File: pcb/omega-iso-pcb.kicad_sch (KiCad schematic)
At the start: 188 parts

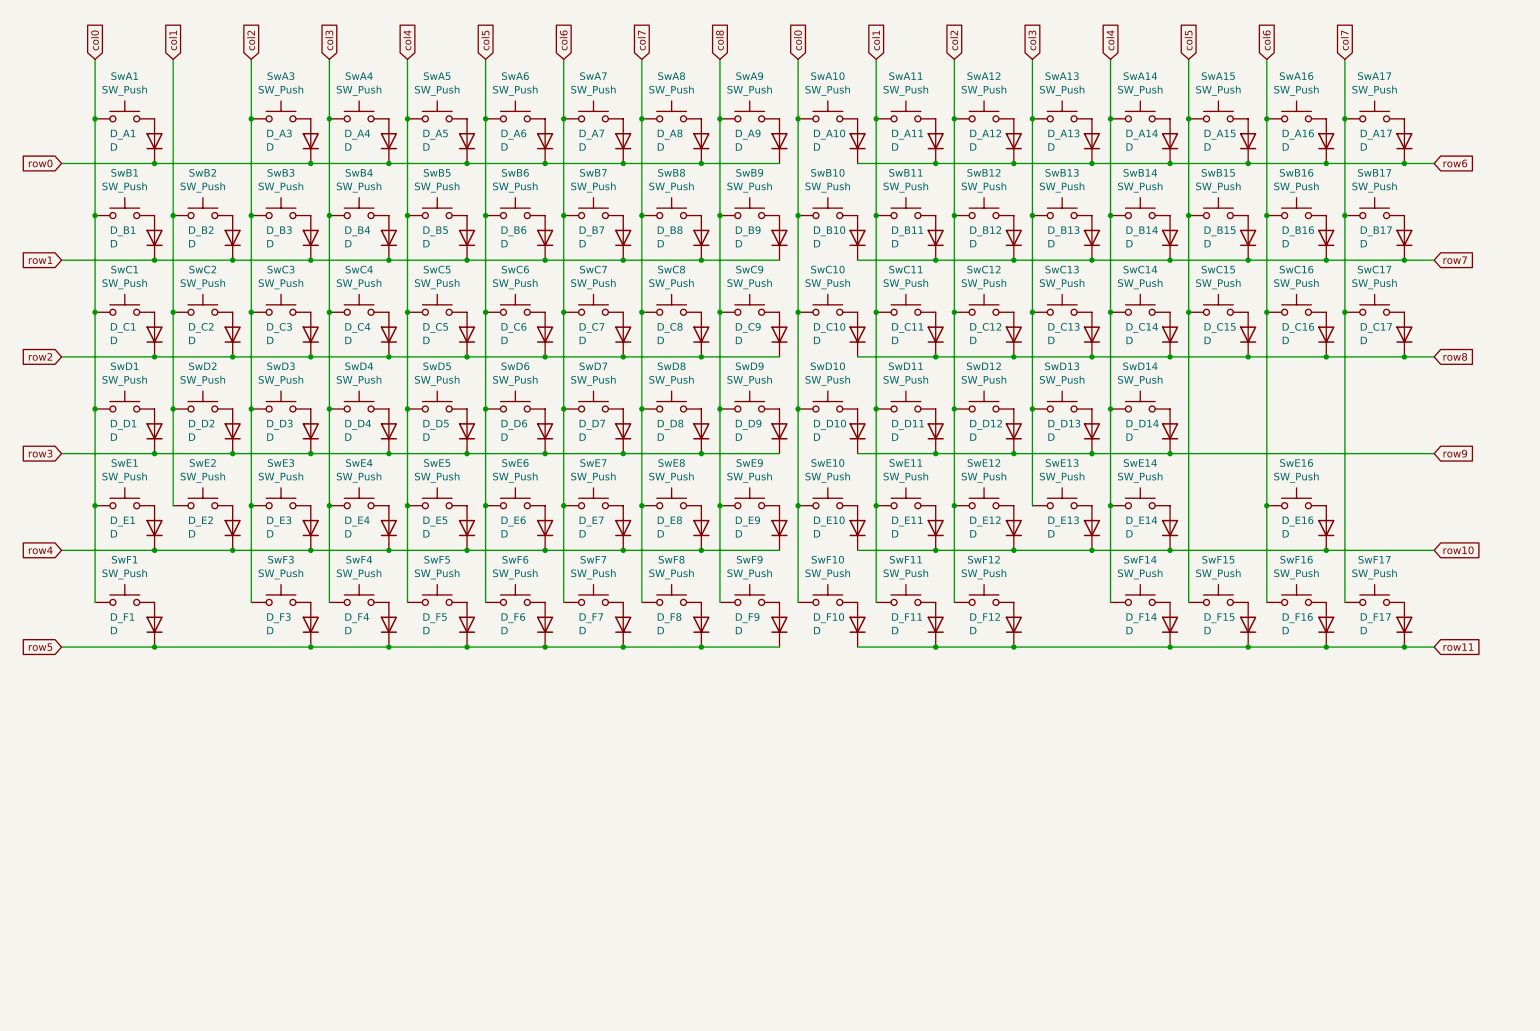
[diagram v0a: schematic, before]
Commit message: OmegaISO v0.9
* WKL TKL-like layout
* Hotswappable
* 4 up facing RGB modules for logo backlight
* Based on the Frood microcontroller
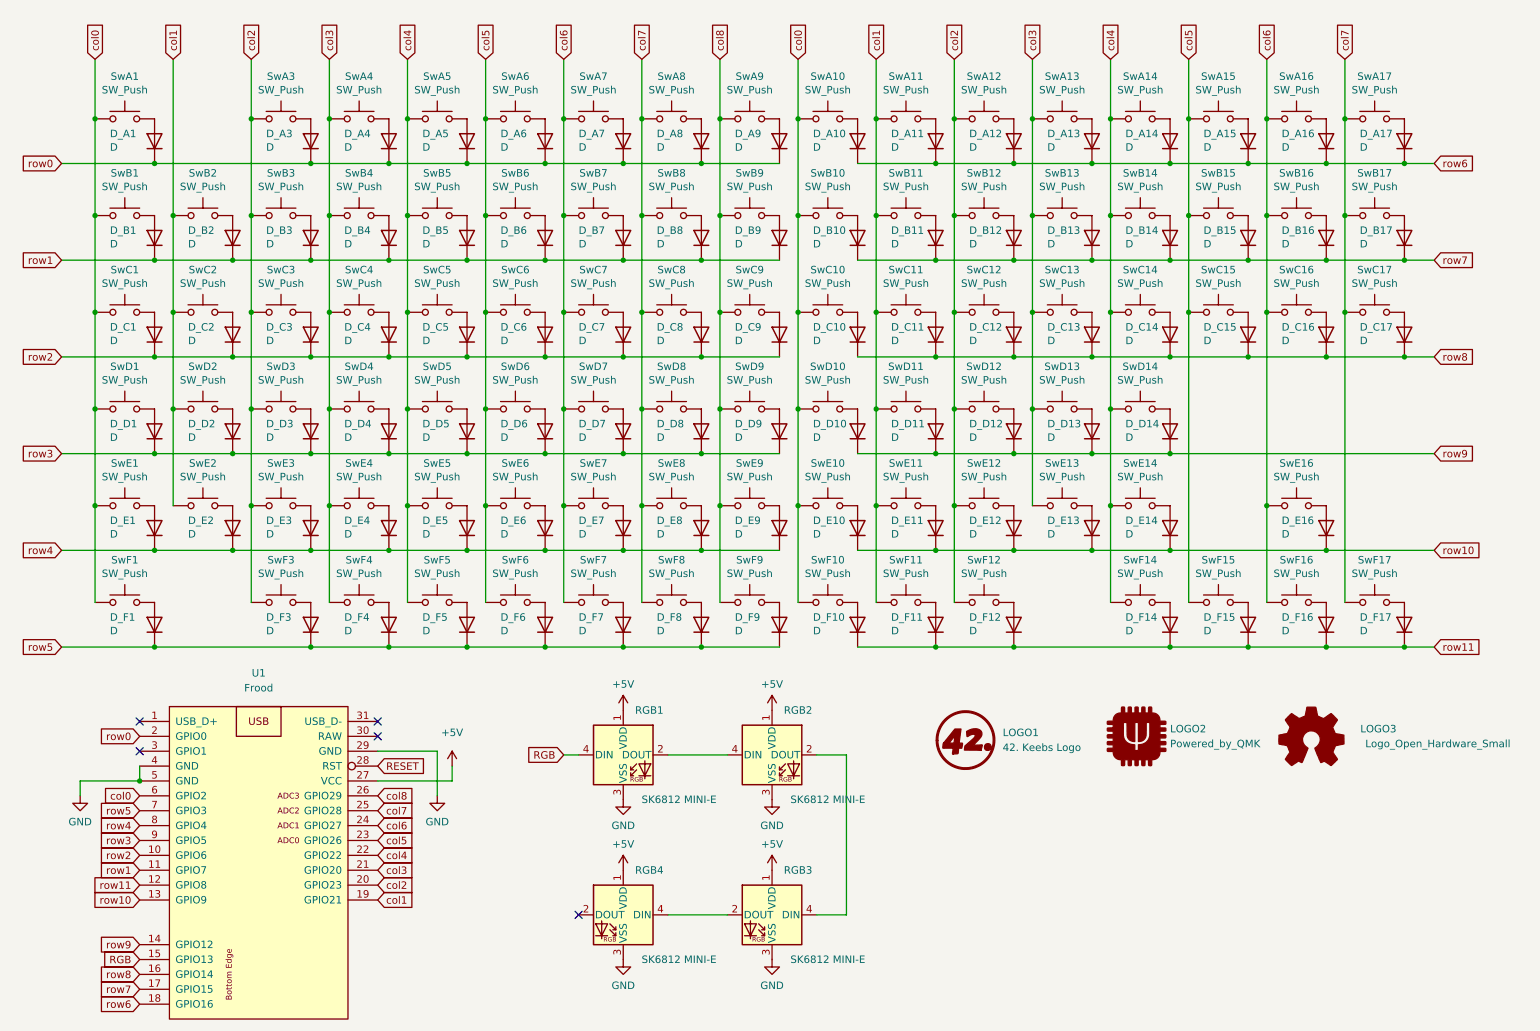
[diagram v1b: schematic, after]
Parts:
- added LOGO1: 42. Keebs Logo, 42keebs:42Keebs-icon-10mm-Mask, symbol 42keebs:42. Keebs Logo
- added LOGO2: Powered_by_QMK, 42keebs:Powered_by_QMK-20mm-SilkS, symbol 42keebs:Powered_by_QMK
- added LOGO3: Logo_Open_Hardware_Small, 42keebs:oshw, symbol Graphic:Logo_Open_Hardware_Small
- added RGB1, RGB2, RGB3, RGB4: SK6812 MINI-E, 42keebs:YS-SK6812MINI-E, symbol LED:WS2812B
- added U1: Frood, 42keebs:Frood_PinHeader_2x13+5_P2.54mm_Labels_Top, symbol 42keebs:Frood
- D_A1, D_A10, D_A11, D_A12, D_A13, D_A14, D_A15, D_A16, D_A17, D_A3, D_A4, D_A5, D_A6, D_A7, D_A8, D_A9, D_B1, D_B10, D_B11, D_B12, D_B13, D_B14, D_B15, D_B16, D_B17, D_B2, D_B3, D_B4, D_B5, D_B6, D_B7, D_B8, D_B9, D_C1, D_C10, D_C11, D_C12, D_C13, D_C14, D_C15, D_C16, D_C17, D_C2, D_C3, D_C4, D_C5, D_C6, D_C7, D_C8, D_C9, D_D1, D_D10, D_D11, D_D12, D_D13, D_D14, D_D2, D_D3, D_D4, D_D5, D_D6, D_D7, D_D8, D_D9, D_E1, D_E10, D_E11, D_E12, D_E13, D_E14, D_E16, D_E2, D_E3, D_E4, D_E5, D_E6, D_E7, D_E8, D_E9, D_F1, D_F10, D_F11, D_F12, D_F14, D_F15, D_F16, D_F17, D_F3, D_F4, D_F5, D_F6, D_F7, D_F8, D_F9: footprint 42keebs:Diode_SOD123_dual_sided -> 42keebs:Diode_THT_SOD123F
- SwA1, SwA10, SwA11, SwA12, SwA13, SwA14, SwA15, SwA16, SwA17, SwA3, SwA4, SwA5, SwA6, SwA7, SwA8, SwA9, SwB1, SwB10, SwB11, SwB12, SwB13, SwB14, SwB15, SwB16, SwB17, SwB2, SwB3, SwB4, SwB5, SwB6, SwB7, SwB8, SwB9, SwC1, SwC10, SwC11, SwC12, SwC13, SwC14, SwC15, SwC16, SwC17, SwC2, SwC3, SwC4, SwC5, SwC6, SwC7, SwC8, SwC9, SwD1, SwD10, SwD11, SwD12, SwD13, SwD14, SwD2, SwD3, SwD4, SwD5, SwD6, SwD7, SwD8, SwD9, SwE1, SwE10, SwE11, SwE12, SwE13, SwE14, SwE16, SwE2, SwE3, SwE4, SwE5, SwE6, SwE7, SwE8, SwE9, SwF1, SwF10, SwF11, SwF12, SwF14, SwF15, SwF16, SwF17, SwF3, SwF4, SwF5, SwF6, SwF7, SwF8, SwF9: footprint 42keebs:Kailh_socket_PG1350 -> MX_Only:MXOnly-ISO-Hotswap-ReversedStabilizers
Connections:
- net col0: now also SwA10.2, SwB1.2, SwB10.2, SwC1.2, SwC10.2, SwD1.2, SwD10.2, SwE1.2, SwE10.2, SwF1.2, SwF10.2, U1.6 (GPIO2); no longer SwA10.1, SwB1.1, SwB10.1, SwC1.1, SwC10.1, SwD1.1, SwD10.1, SwE1.1, SwE10.1, SwF1.1, SwF10.1
- net col1: now also U1.19 (GPIO21)
- net col2: now also SwA3.2, U1.20 (GPIO23); no longer SwA3.1
- net col3: now also U1.21 (GPIO20)
- net col4: now also U1.22 (GPIO22)
- net col5: now also U1.23 (GPIO26)
- net col6: now also U1.24 (GPIO27)
- net col7: now also U1.25 (GPIO28)
- net col8: now also U1.26 (GPIO29)
- net row0: now also U1.2 (GPIO0)
- net row1: now also U1.11 (GPIO7)
- net row10: now also U1.13 (GPIO9)
- net row11: now also U1.12 (GPIO8)
- net row2: now also U1.10 (GPIO6)
- net row3: now also U1.9 (GPIO5)
- net row4: now also U1.8 (GPIO4)
- net row5: now also U1.7 (GPIO3)
- net row6: now also U1.18 (GPIO16)
- net row7: now also U1.17 (GPIO15)
- net row8: now also U1.16 (GPIO14)
- net row9: now also U1.14 (GPIO12)
- net at D_E1.2 (A): now also SwE1.1; no longer SwE1.2
- net at D_B1.2 (A): now also SwB1.1; no longer SwB1.2
- net at D_F10.2 (A): now also SwF10.1; no longer SwF10.2
- net at D_B10.2 (A): now also SwB10.1; no longer SwB10.2
- net at D_C1.2 (A): now also SwC1.1; no longer SwC1.2
- net at D_F1.2 (A): now also SwF1.1; no longer SwF1.2
- net at D_A10.2 (A): now also SwA10.1; no longer SwA10.2
- net at D_A3.2 (A): now also SwA3.1; no longer SwA3.2
- net at D_D1.2 (A): now also SwD1.1; no longer SwD1.2
- net at D_E10.2 (A): now also SwE10.1; no longer SwE10.2
- net at D_C10.2 (A): now also SwC10.1; no longer SwC10.2
- net at D_D10.2 (A): now also SwD10.1; no longer SwD10.2
- new net: RGB1.2 (DOUT), RGB2.4 (DIN)
- new net: RGB2.2 (DOUT), RGB3.4 (DIN)
- new net: RGB3.2 (DOUT), RGB4.4 (DIN)
- new net +5V: RGB1.1 (VDD), RGB2.1 (VDD), RGB3.1 (VDD), RGB4.1 (VDD), U1.27 (VCC)
- new net GND: RGB1.3 (VSS), RGB2.3 (VSS), RGB3.3 (VSS), RGB4.3 (VSS), U1.29 (GND), U1.4 (GND), U1.5 (GND)
- new net RESET: U1.28 (RST)
- new net RGB: RGB1.4 (DIN), U1.15 (GPIO13)
- no-connect marks 0 -> 5
